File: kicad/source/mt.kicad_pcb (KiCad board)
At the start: 2 copper layers, 18 parts, among them IC1 MSPM0G3507SPMR, IC2 DAC082S085CIMMX_NOPB, IC3 IS62WV1288BLL-55QLI, IC4 MCP73831T-2ACI_OT, IC5 RT9167A-33GB, IC6 SN74HC148NSR, IC7 TLV9152IDR, IC8 TPS613222ADBVR, IC9 BQ29728DSER, J1 694106301002, J2 SJ1-3524N, Q1 CSD16406Q3, Q2 CSD16406Q3, U1 1043

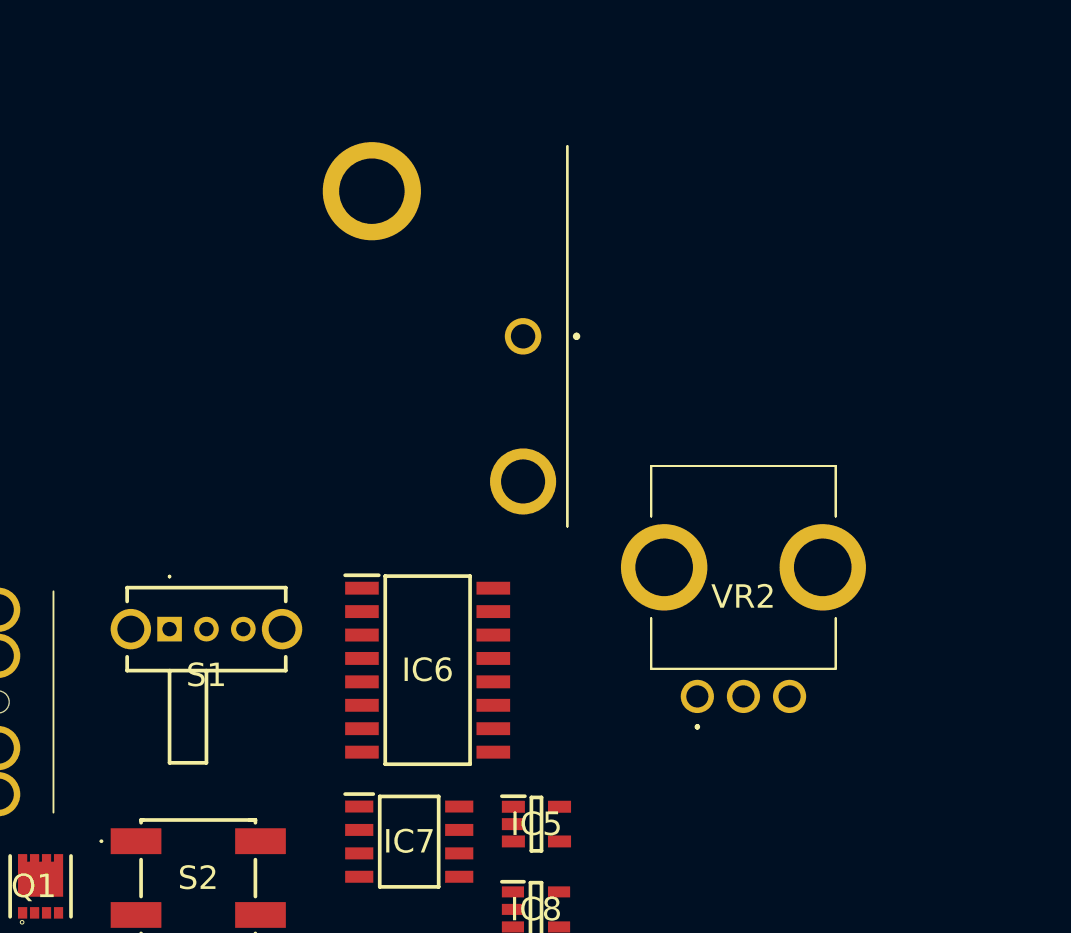
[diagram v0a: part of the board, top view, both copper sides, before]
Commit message: completed power electronics schematic
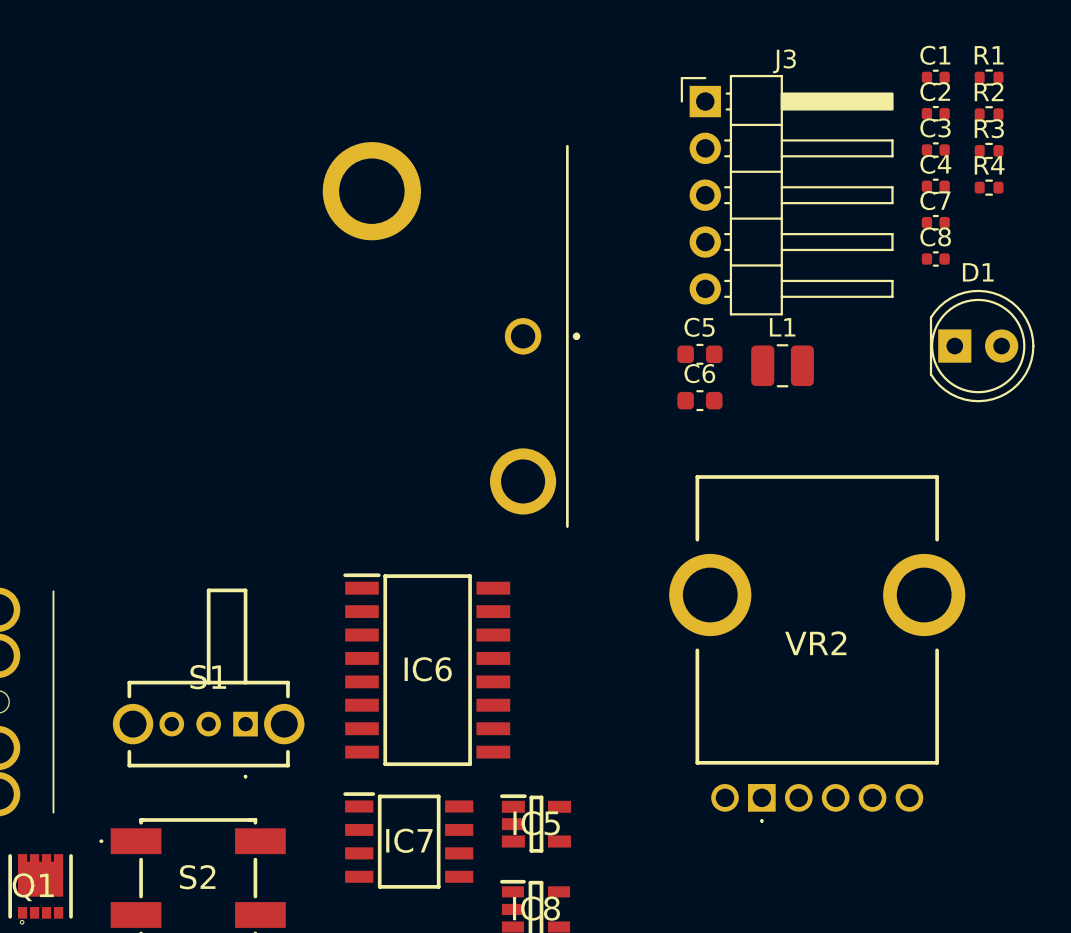
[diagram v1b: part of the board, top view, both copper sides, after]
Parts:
- added C1: 4.7u, Capacitor_SMD:C_0402_1005Metric, F.Cu at (205.4, 44.4)
- added C2: 4.7u, Capacitor_SMD:C_0402_1005Metric, F.Cu at (205.4, 46.4)
- added C3: 0.1u, Capacitor_SMD:C_0402_1005Metric, F.Cu at (205.4, 48.4)
- added C4: 4.7u, Capacitor_SMD:C_0402_1005Metric, F.Cu at (205.4, 50.3)
- added C5: 22u, Capacitor_SMD:C_0603_1608Metric, F.Cu at (192.6, 59.5)
- added C6: 22u, Capacitor_SMD:C_0603_1608Metric, F.Cu at (192.6, 62.0)
- added C7: 4.7u, Capacitor_SMD:C_0402_1005Metric, F.Cu at (205.4, 52.3)
- added C8: 0.1u, Capacitor_SMD:C_0402_1005Metric, F.Cu at (205.4, 54.3)
- added D1: LED, LED_THT:LED_D5.0mm, F.Cu at (206.5, 59.0)
- added J3: Conn_01x05_MountingPin, Connector_PinHeader_2.54mm:PinHeader_1x05_P2.54mm_Horizontal, F.Cu at (192.9, 45.7)
- added L1: 2.2u, Inductor_SMD:L_1008_2520Metric, F.Cu at (197.1, 60.1)
- added R1: 4.7k, Resistor_SMD:R_0402_1005Metric, F.Cu at (208.3, 44.4)
- added R2: 2k, Resistor_SMD:R_0402_1005Metric, F.Cu at (208.3, 46.4)
- added R3: 2.2k, Resistor_SMD:R_0402_1005Metric, F.Cu at (208.3, 48.4)
- added R4: 330, Resistor_SMD:R_0402_1005Metric, F.Cu at (208.3, 50.4)
- VR2: value PTV09A-4020F-C103 -> PTV112-4420A-C104; footprint PTV09A-4020F-C103:PTV09A4020FC103 -> PTV112-4420A-C104:PTV1124420AC104
- moved S1 6.60 mm to (168.0, 79.5), turned to 180 degrees
- moved VR2 6.52 mm to (196.0, 83.5)
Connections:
- IC4 pad 1: unconnected-(IC4-STAT-Pad1) -> Net-(IC4-STAT)
- IC4 pad 2: unconnected-(IC4-VSS-Pad2) -> GND
- IC4 pad 3: unconnected-(IC4-VBAT-Pad3) -> CELL+
- IC4 pad 4: unconnected-(IC4-VDD-Pad4) -> Net-(D1-A)
- IC4 pad 5: unconnected-(IC4-PROG-Pad5) -> Net-(IC4-PROG)
- IC5 pad 1: unconnected-(IC5-VIN-Pad1) -> Net-(IC5-EN)
- IC5 pad 2: unconnected-(IC5-GND-Pad2) -> GND
- IC5 pad 3: unconnected-(IC5-EN-Pad3) -> Net-(IC5-EN)
- IC5 pad 4: unconnected-(IC5-BP-Pad4) -> Net-(IC5-BP)
- IC5 pad 5: unconnected-(IC5-VOUT-Pad5) -> Net-(IC5-VOUT)
- IC8 pad 1: unconnected-(IC8-SW-Pad1) -> Net-(IC8-SW)
- IC8 pad 2: unconnected-(IC8-GND-Pad2) -> GND
- IC8 pad 4: unconnected-(IC8-VOUT-Pad4) -> Net-(IC5-EN)
- IC9 pad 2: unconnected-(IC9-COUT-Pad2) -> Net-(IC9-COUT)
- IC9 pad 3: unconnected-(IC9-DOUT-Pad3) -> Net-(IC9-DOUT)
- IC9 pad 4: unconnected-(IC9-VSS-Pad4) -> Net-(IC9-VSS)
- IC9 pad 5: unconnected-(IC9-BAT-Pad5) -> Net-(IC9-BAT)
- IC9 pad 6: unconnected-(IC9-V--Pad6) -> Net-(IC9-V-)
- J1 pad 1: unconnected-(J1-POWER-Pad1) -> Net-(D1-A)
- J1 pad 2: unconnected-(J1-GND_1-Pad2) -> GND
- J1 pad 3: unconnected-(J1-GND_2-Pad3) -> GND
- Q1 pad 1: Net-(Q1-S_1) -> GND
- Q1 pad 2: Net-(Q1-S_1) -> GND
- Q1 pad 3: Net-(Q1-S_1) -> GND
- Q1 pad 4: unconnected-(Q1-G-Pad4) -> Net-(IC9-COUT)
- Q2 pad 1: Net-(Q2-S_1) -> Net-(IC9-VSS)
- Q2 pad 2: Net-(Q2-S_1) -> Net-(IC9-VSS)
- Q2 pad 3: Net-(Q2-S_1) -> Net-(IC9-VSS)
- Q2 pad 4: unconnected-(Q2-G-Pad4) -> Net-(IC9-DOUT)
- Q2 pad 5: Net-(Q2-D_1) -> Net-(Q1-D_1)
- Q2 pad 6: Net-(Q2-D_1) -> Net-(Q1-D_1)
- Q2 pad 7: Net-(Q2-D_1) -> Net-(Q1-D_1)
- Q2 pad 8: Net-(Q2-D_1) -> Net-(Q1-D_1)
- S1 pad 2: unconnected-(S1-Pad2) -> VBAT
- S1 pad 3: unconnected-(S1-Pad3) -> CELL+
- S2 pad 1: unconnected-(S2-Pad1) -> Net-(S2-Pad1)
- S2 pad 2: unconnected-(S2-Pad2) -> Net-(S2-Pad1)
- S2 pad 3: unconnected-(S2-Pad3) -> Net-(S2-Pad3)
- S2 pad 4: unconnected-(S2-Pad4) -> Net-(S2-Pad3)
- U1 pad 1: unconnected-(U1-+-Pad1) -> CELL+
- U1 pad 2: unconnected-(U1---Pad2) -> Net-(IC9-VSS)

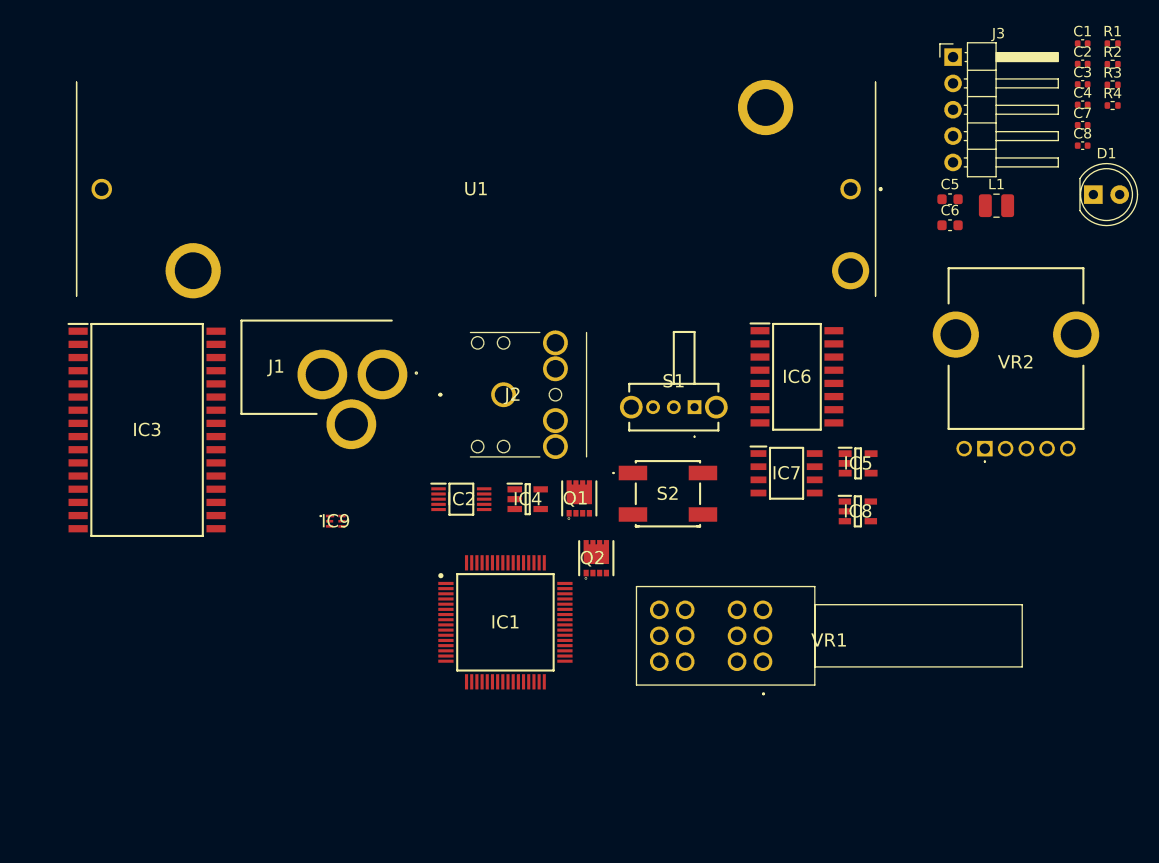
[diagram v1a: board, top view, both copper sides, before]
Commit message: revised audio electronics volume pot
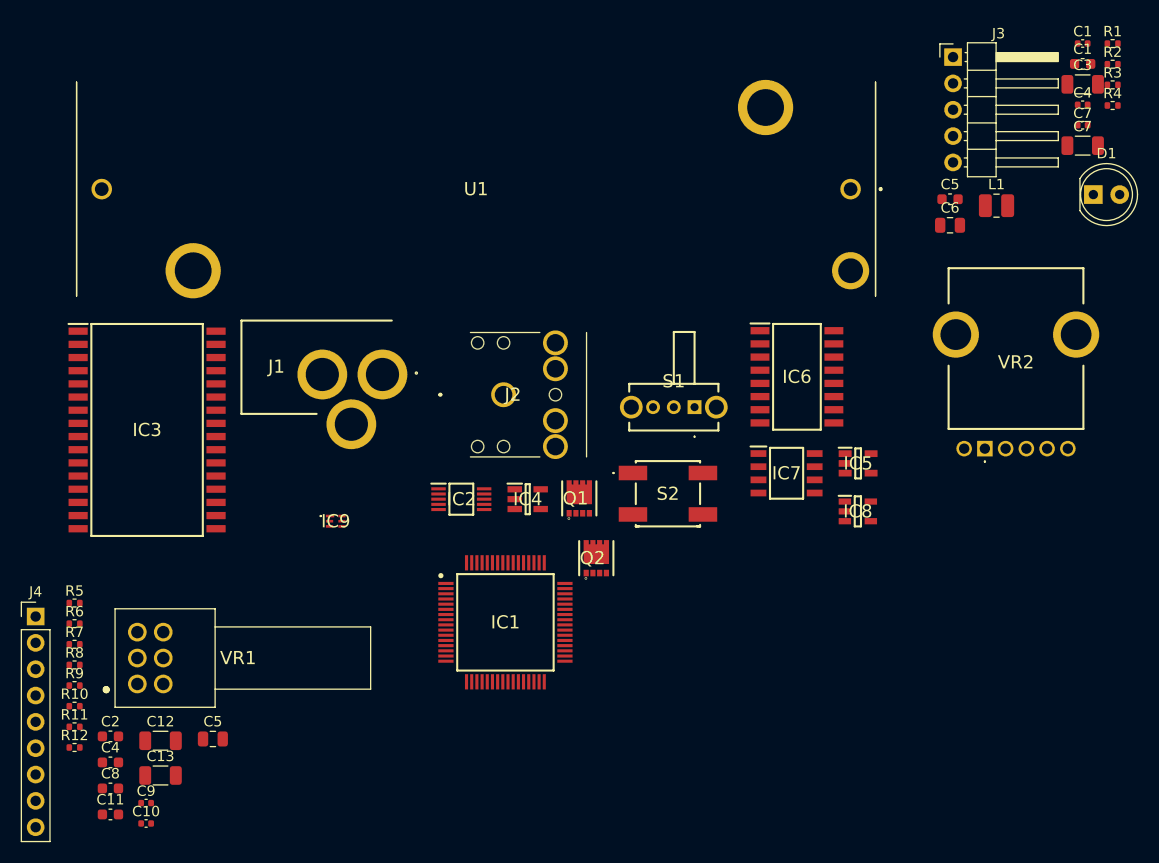
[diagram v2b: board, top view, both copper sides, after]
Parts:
- added C10: 4.7n, Capacitor_SMD:C_0402_1005Metric, F.Cu at (115.1, 119.7)
- added C11: 10u, Capacitor_SMD:C_0603_1608Metric, F.Cu at (111.7, 118.8)
- added C12: 100n, Capacitor_SMD:C_1206_3216Metric, F.Cu at (116.5, 111.7)
- added C13: 100n, Capacitor_SMD:C_1206_3216Metric, F.Cu at (116.5, 115.0)
- added C2: 10u, Capacitor_SMD:C_0603_1608Metric, F.Cu at (111.7, 111.2)
- added C4: 10u, Capacitor_SMD:C_0603_1608Metric, F.Cu at (111.7, 113.8)
- added C5: 47u, Capacitor_SMD:C_0805_2012Metric, F.Cu at (121.5, 111.5)
- added C8: 10u, Capacitor_SMD:C_0603_1608Metric, F.Cu at (111.7, 116.3)
- added C9: 4.7n, Capacitor_SMD:C_0402_1005Metric, F.Cu at (115.1, 117.7)
- added J4: Conn_01x09_MountingPin, Connector_PinHeader_2.54mm:PinHeader_1x09_P2.54mm_Vertical, F.Cu at (104.5, 99.7)
- added R10: 100k, Resistor_SMD:R_0402_1005Metric, F.Cu at (108.2, 108.3)
- added R11: 10k, Resistor_SMD:R_0402_1005Metric, F.Cu at (108.2, 110.3)
- added R12: 10k, Resistor_SMD:R_0402_1005Metric, F.Cu at (108.2, 112.3)
- added R5: 10k, Resistor_SMD:R_0402_1005Metric, F.Cu at (108.2, 98.4)
- added R6: 10k, Resistor_SMD:R_0402_1005Metric, F.Cu at (108.2, 100.4)
- added R7: 10k, Resistor_SMD:R_0402_1005Metric, F.Cu at (108.2, 102.4)
- added R8: 10k, Resistor_SMD:R_0402_1005Metric, F.Cu at (108.2, 104.4)
- added R9: 100k, Resistor_SMD:R_0402_1005Metric, F.Cu at (108.2, 106.3)
- C1: renamed from C2; value 4.7u -> 10u; footprint Capacitor_SMD:C_0402_1005Metric -> Capacitor_SMD:C_0603_1608Metric
- C3: value 0.1u -> 100n; footprint Capacitor_SMD:C_0402_1005Metric -> Capacitor_SMD:C_1206_3216Metric
- C6: value 22u -> 47u; footprint Capacitor_SMD:C_0603_1608Metric -> Capacitor_SMD:C_0805_2012Metric
- C7: renamed from C8; value 0.1u -> 100n; footprint Capacitor_SMD:C_0402_1005Metric -> Capacitor_SMD:C_1206_3216Metric
- VR1: value PTD904-1020K-A103 -> PTD902-2015F-A103; footprint PTD904-1020K-A103:PTD9041020KA103 -> PTD902-2015F-A103:PTD9022015FA103
- moved VR1 60.4 mm to (114.3, 106.2)
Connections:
- IC2 pad 2: unconnected-(IC2-VOUTA-Pad2) -> DACL
- IC2 pad 3: unconnected-(IC2-VOUTB-Pad3) -> DACR
- IC5 pad 5: Net-(IC5-VOUT) -> VDD
- IC7 pad 1: unconnected-(IC7-OUT1-Pad1) -> L
- IC7 pad 2: unconnected-(IC7-IN1--Pad2) -> RV1A
- IC7 pad 3: unconnected-(IC7-IN1+-Pad3) -> Net-(IC7-IN1+)
- IC7 pad 4: unconnected-(IC7-V--Pad4) -> GND
- IC7 pad 5: unconnected-(IC7-IN2+-Pad5) -> Net-(IC7-IN2+)
- IC7 pad 6: unconnected-(IC7-IN2--Pad6) -> RV2A
- IC7 pad 7: unconnected-(IC7-OUT2-Pad7) -> R
- IC7 pad 8: unconnected-(IC7-V+-Pad8) -> VDD
- J2 pad 1: unconnected-(J2-SLEEVE-Pad1) -> GND
- J2 pad 2: unconnected-(J2-TIP-Pad2) -> Net-(J2-TIP)
- J2 pad 3: unconnected-(J2-RING-Pad3) -> Net-(J2-RING)
- VR2 pad A1: unconnected-(VR2-PadA1) -> DACL
- VR2 pad A2: unconnected-(VR2-PadA2) -> Net-(C9-Pad1)
- VR2 pad B1: unconnected-(VR2-PadB1) -> Net-(C10-Pad1)
- VR2 pad B2: unconnected-(VR2-PadB2) -> DACR

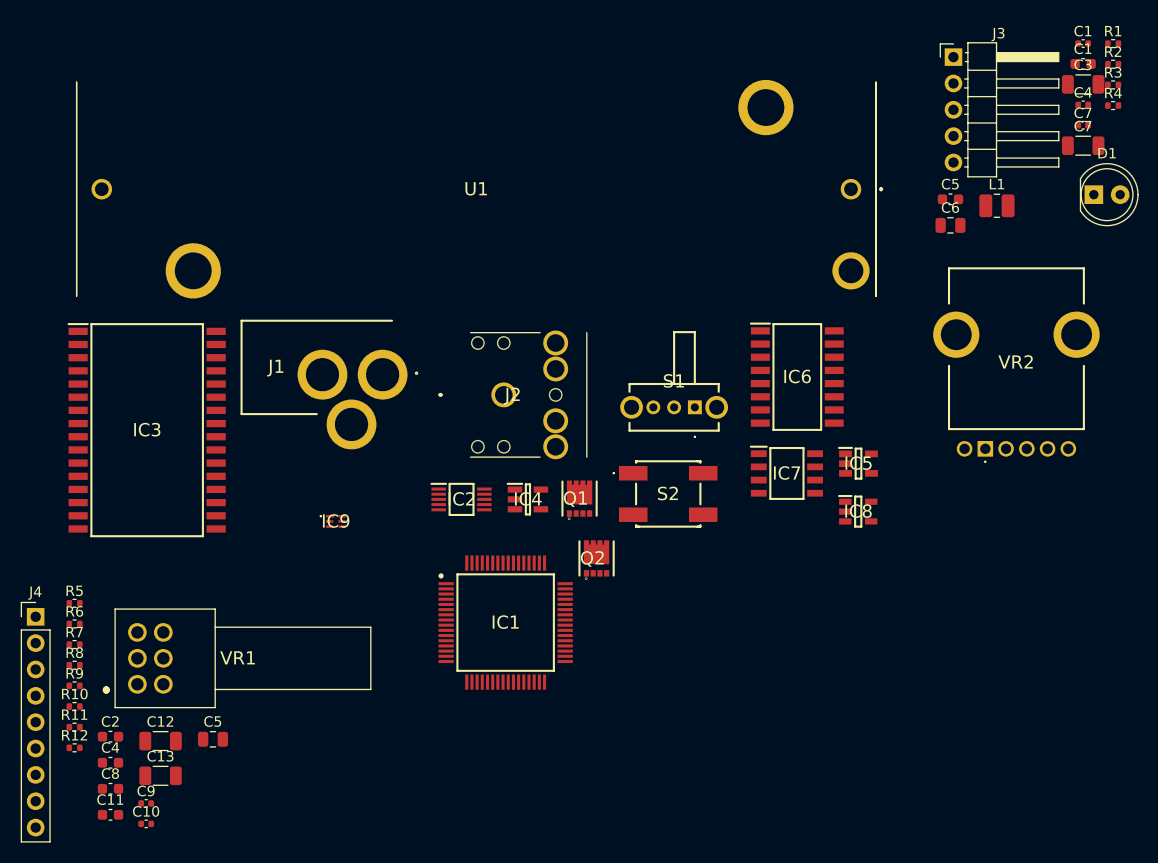
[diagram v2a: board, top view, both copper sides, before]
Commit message: simplified power electronics
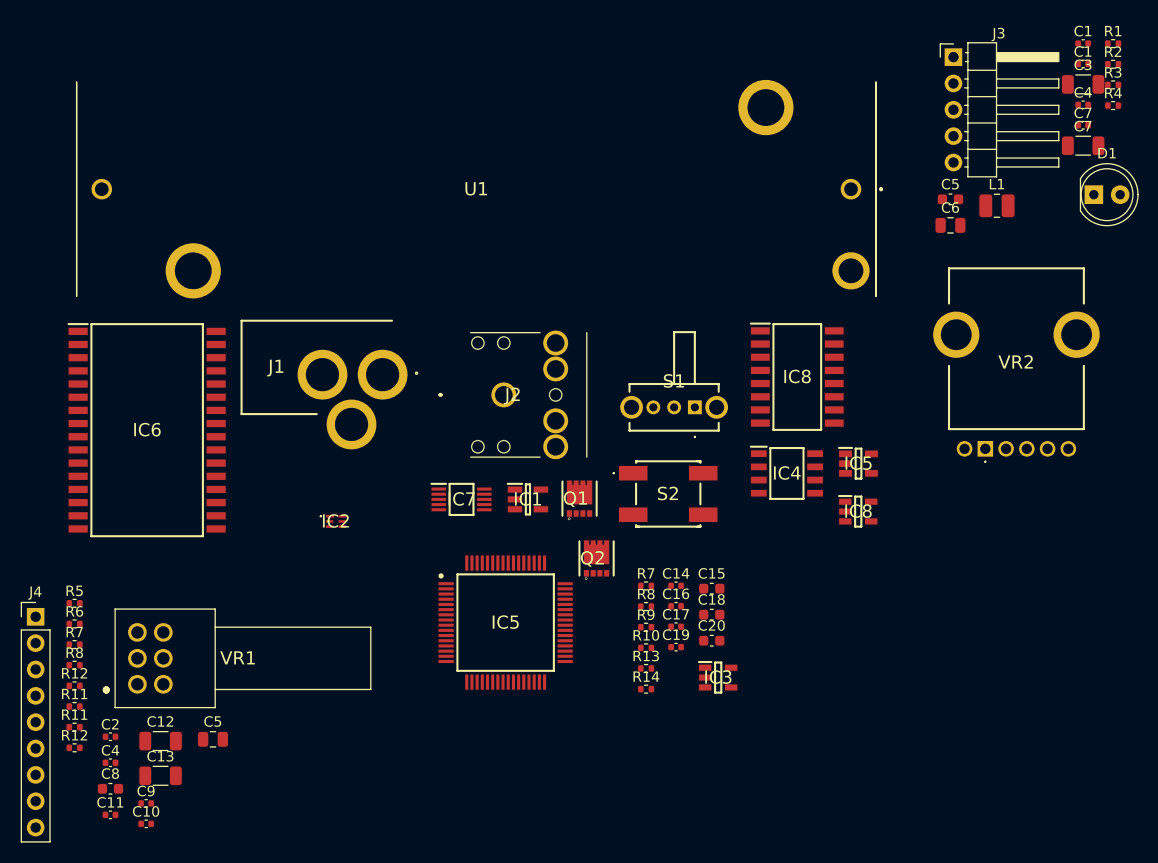
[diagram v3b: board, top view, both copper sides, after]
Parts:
- added C14: 10n, Capacitor_SMD:C_0402_1005Metric, F.Cu at (166.2, 96.7)
- added C15: 22u, Capacitor_SMD:C_0603_1608Metric, F.Cu at (169.6, 97.0)
- added C16: 10u, Capacitor_SMD:C_0402_1005Metric, F.Cu at (166.2, 98.7)
- added C17: 10u, Capacitor_SMD:C_0402_1005Metric, F.Cu at (166.2, 100.6)
- added C18: 22u, Capacitor_SMD:C_0603_1608Metric, F.Cu at (169.6, 99.5)
- added C19: 10u, Capacitor_SMD:C_0402_1005Metric, F.Cu at (166.2, 102.6)
- added C20: 22u, Capacitor_SMD:C_0603_1608Metric, F.Cu at (169.6, 102.0)
- added IC3: TLV74333PDBVR, TLV74333PDBVR:SOT95P280X145-5N, F.Cu at (170.2, 105.5)
- added R10: 100k, Resistor_SMD:R_0402_1005Metric, F.Cu at (163.3, 102.7)
- added R13: 100k, Resistor_SMD:R_0402_1005Metric, F.Cu at (163.3, 104.7)
- added R14: 100k, Resistor_SMD:R_0402_1005Metric, F.Cu at (163.3, 106.7)
- added R7: 100k, Resistor_SMD:R_0402_1005Metric, F.Cu at (163.3, 96.7)
- added R8: 100k, Resistor_SMD:R_0402_1005Metric, F.Cu at (163.3, 98.7)
- added R9: 100k, Resistor_SMD:R_0402_1005Metric, F.Cu at (163.3, 100.7)
- C1, C11, C2, C4: footprint Capacitor_SMD:C_0603_1608Metric -> Capacitor_SMD:C_0402_1005Metric
- renumbered IC4 to IC1, IC9 to IC2, IC7 to IC4, IC1 to IC5, IC3 to IC6, IC2 to IC7, IC6 to IC8, R10 to R11, R9 to R12
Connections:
- IC4 pad 3: Net-(IC7-IN1+) -> Net-(IC4-IN1+)
- IC4 pad 5: Net-(IC7-IN2+) -> Net-(IC4-IN2+)
- IC5 pad 1: unconnected-(IC1-PB13-Pad1) -> A13
- IC5 pad 12: unconnected-(IC1-PA19_/_SWDIO-Pad12) -> SWDIO
- IC5 pad 13: unconnected-(IC1-PA20_/_SWCLK-Pad13) -> SWCLK
- IC5 pad 2: unconnected-(IC1-PB14-Pad2) -> A14
- IC5 pad 3: unconnected-(IC1-PB15-Pad3) -> A15
- IC5 pad 32: unconnected-(IC1-VCORE-Pad32) -> Net-(IC5-VCORE)
- IC5 pad 38: unconnected-(IC1-NRST-Pad38) -> NRST
- IC5 pad 4: unconnected-(IC1-PB16-Pad4) -> A16
- IC5 pad 40: unconnected-(IC1-VDD-Pad40) -> Net-(IC5-VDD)
- IC5 pad 41: unconnected-(IC1-VSS-Pad41) -> GND
- IC5 pad 47: unconnected-(IC1-PB0-Pad47) -> A0
- IC5 pad 48: unconnected-(IC1-PB1-Pad48) -> A1
- IC5 pad 50: unconnected-(IC1-PB2-Pad50) -> A2
- IC5 pad 51: unconnected-(IC1-PB3-Pad51) -> A3
- IC5 pad 52: unconnected-(IC1-PB4-Pad52) -> A4
- IC5 pad 53: unconnected-(IC1-PB5-Pad53) -> A5
- IC5 pad 58: unconnected-(IC1-PB6-Pad58) -> A6
- IC5 pad 59: unconnected-(IC1-PB7-Pad59) -> A7
- IC5 pad 60: unconnected-(IC1-PB8-Pad60) -> A8
- IC5 pad 61: unconnected-(IC1-PB9-Pad61) -> A9
- IC5 pad 62: unconnected-(IC1-PB10-Pad62) -> A10
- IC5 pad 63: unconnected-(IC1-PB11_/_CLK_OUT-Pad63) -> A11
- IC5 pad 64: unconnected-(IC1-PB12-Pad64) -> A12
- IC6 pad 10: unconnected-(IC3-A2-Pad10) -> A2
- IC6 pad 11: unconnected-(IC3-A1-Pad11) -> A1
- IC6 pad 12: unconnected-(IC3-A0-Pad12) -> A0
- IC6 pad 16: unconnected-(IC3-GND-Pad16) -> GND
- IC6 pad 2: unconnected-(IC3-A16-Pad2) -> A16
- IC6 pad 23: unconnected-(IC3-A10-Pad23) -> A10
- IC6 pad 25: unconnected-(IC3-A11-Pad25) -> A11
- IC6 pad 26: unconnected-(IC3-A9-Pad26) -> A9
- IC6 pad 27: unconnected-(IC3-A8-Pad27) -> A8
- IC6 pad 28: unconnected-(IC3-A13-Pad28) -> A13
- IC6 pad 3: unconnected-(IC3-A14-Pad3) -> A14
- IC6 pad 31: unconnected-(IC3-A15-Pad31) -> A15
- IC6 pad 32: unconnected-(IC3-VDD-Pad32) -> Net-(IC6-VDD)
- IC6 pad 4: unconnected-(IC3-A12-Pad4) -> A12
- IC6 pad 5: unconnected-(IC3-A7-Pad5) -> A7
- IC6 pad 6: unconnected-(IC3-A6-Pad6) -> A6
- IC6 pad 7: unconnected-(IC3-A5-Pad7) -> A5
- IC6 pad 8: unconnected-(IC3-A4-Pad8) -> A4
- IC6 pad 9: unconnected-(IC3-A3-Pad9) -> A3
- J3 pad 1: unconnected-(J3-Pin_1-Pad1) -> GND
- J3 pad 2: unconnected-(J3-Pin_2-Pad2) -> VDD
- J3 pad 3: unconnected-(J3-Pin_3-Pad3) -> NRST
- J3 pad 4: unconnected-(J3-Pin_4-Pad4) -> SWDIO
- J3 pad 5: unconnected-(J3-Pin_5-Pad5) -> SWCLK
- S2 pad 3: Net-(S2-Pad3) -> GND
- S2 pad 4: Net-(S2-Pad3) -> GND
